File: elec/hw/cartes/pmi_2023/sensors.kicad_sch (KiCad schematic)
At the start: 44 parts, among them SW1 TQ2537A, SW2 TQ2537, SW6 TQ2537, SW9 TQ2537A, U10 tof_sensor_master, U13 GP2S60B, U14 GP2S60B, U15 GP2S60B, U16 GP2S60B, U19 GP2S60B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

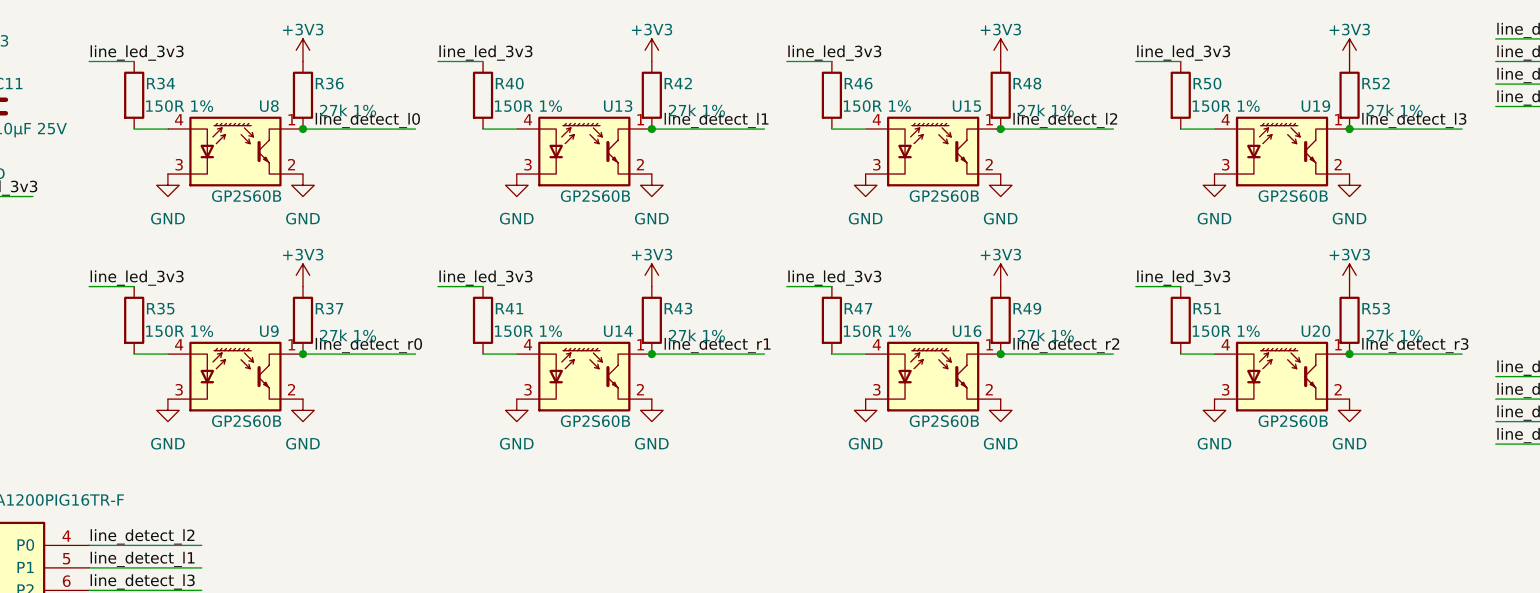
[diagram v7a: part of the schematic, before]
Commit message: GP2S60B replaced by ITR1204SR10A, RGB LED replaced by NH-B2020RGBA
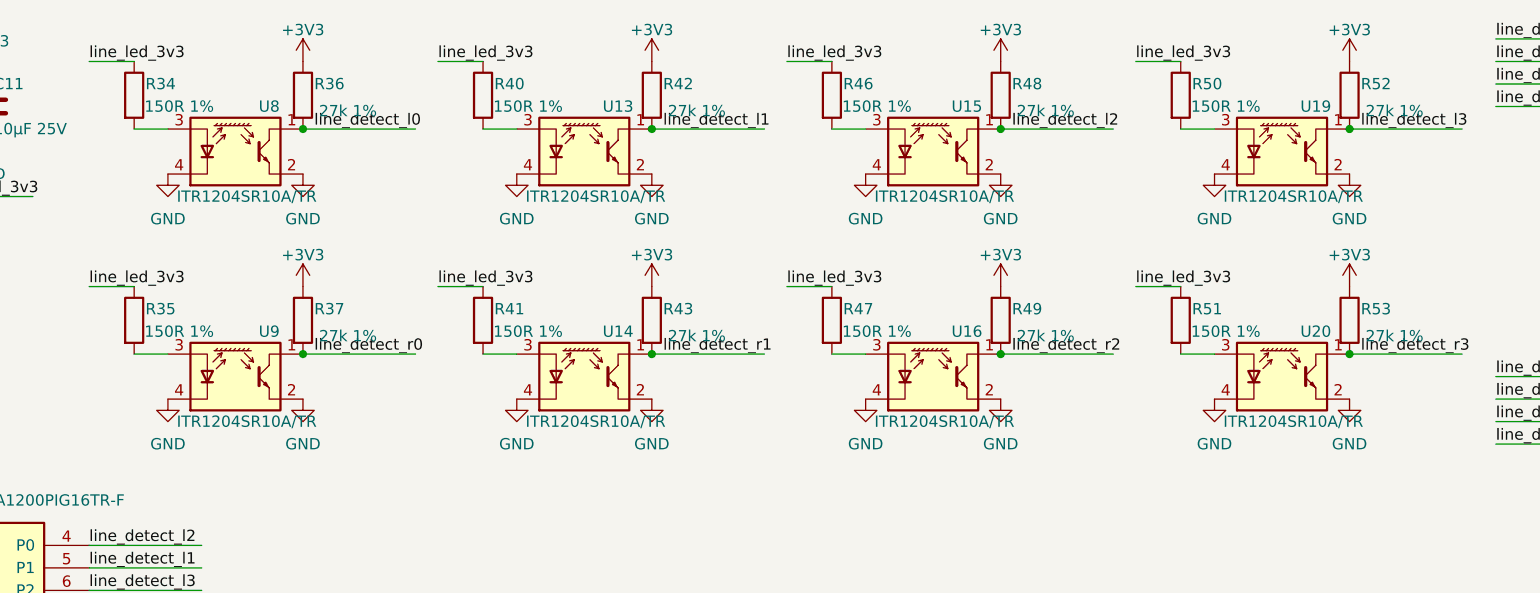
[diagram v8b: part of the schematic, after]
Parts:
- U13, U14, U15, U16, U19, U20, U8, U9: value GP2S60B -> ITR1204SR10A/TR; footprint cocotter_ic:GP2S60 -> cocotter_ic:ITR1204SR10A; symbol cocotter_ic:GP2S60B -> cocotter_ic:ITR1204SR10A/TR; JLCPCB C83485 -> C2943466
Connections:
- net GND: now also U13.4 (K), U14.4 (K), U15.4 (K), U16.4 (K), U19.4 (K), U20.4 (K), U8.4 (K), U9.4 (K); no longer U13.3 (K), U14.3 (K), U15.3 (K), U16.3 (K), U19.3 (K), U20.3 (K), U8.3 (K), U9.3 (K)
- net at R35.2: now also U9.3 (A); no longer U9.4 (A)
- net at R40.2: now also U13.3 (A); no longer U13.4 (A)
- net at R50.2: now also U19.3 (A); no longer U19.4 (A)
- net at R51.2: now also U20.3 (A); no longer U20.4 (A)
- net at R41.2: now also U14.3 (A); no longer U14.4 (A)
- net at R34.2: now also U8.3 (A); no longer U8.4 (A)
- net at R47.2: now also U16.3 (A); no longer U16.4 (A)
- net at R46.2: now also U15.3 (A); no longer U15.4 (A)
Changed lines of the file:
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@@
 	)
 	(symbol
-		(lib_id "cocotter_ic:GP2S60B")
+		(lib_id "cocotter_ic:ITR1204SR10A/TR")
 		(at 101.6 53.34 0)
 		(unit 1)
@@
 			)
 		)
-		(property "Value" "GP2S60B"
+		(property "Value" "ITR1204SR10A/TR"
 			(at 102.87 58.42 0)
 			(effects
@@
 			)
 		)
-		(property "Footprint" "cocotter_ic:GP2S60"
+		(property "Footprint" "cocotter_ic:ITR1204SR10A"
 			(at 101.6 53.34 0)
 			(effects
@@
 			)
 		)
-		(property "JLCPCB" "C83485"
+		(property "JLCPCB" "C2943466"
 			(at 101.6 53.34 0)
 			(effects
@@
 	)
 	(symbol
-		(lib_id "cocotter_ic:GP2S60B")
+		(lib_id "cocotter_ic:ITR1204SR10A/TR")
 		(at 140.97 27.94 0)
 		(unit 1)
@@
 			)
 		)
-		(property "Value" "GP2S60B"
+		(property "Value" "ITR1204SR10A/TR"
 			(at 142.24 33.02 0)
 			(effects
@@
 			)
 		)
-		(property "Footprint" "cocotter_ic:GP2S60"
+		(property "Footprint" "cocotter_ic:ITR1204SR10A"
 			(at 140.97 27.94 0)
 			(effects
@@
 			)
 		)
-		(property "JLCPCB" "C83485"
+		(property "JLCPCB" "C2943466"
 			(at 140.97 27.94 0)
 			(effects
@@
 	)
 	(symbol
-		(lib_id "cocotter_ic:GP2S60B")
+		(lib_id "cocotter_ic:ITR1204SR10A/TR")
 		(at 219.71 53.34 0)
 		(unit 1)
@@
 			)
 		)
-		(property "Value" "GP2S60B"
+		(property "Value" "ITR1204SR10A/TR"
 			(at 220.98 58.42 0)
 			(effects
@@
 			)
 		)
-		(property "Footprint" "cocotter_ic:GP2S60"
+		(property "Footprint" "cocotter_ic:ITR1204SR10A"
 			(at 219.71 53.34 0)
 			(effects
@@
 			)
 		)
-		(property "JLCPCB" "C83485"
+		(property "JLCPCB" "C2943466"
 			(at 219.71 53.34 0)
 			(effects
@@
 	)
 	(symbol
-		(lib_id "cocotter_ic:GP2S60B")
+		(lib_id "cocotter_ic:ITR1204SR10A/TR")
 		(at 219.71 27.94 0)
 		(unit 1)
@@
 			)
 		)
-		(property "Value" "GP2S60B"
+		(property "Value" "ITR1204SR10A/TR"
 			(at 220.98 33.02 0)
 			(effects
@@
 			)
 		)
-		(property "Footprint" "cocotter_ic:GP2S60"
+		(property "Footprint" "cocotter_ic:ITR1204SR10A"
 			(at 219.71 27.94 0)
 			(effects
@@
 			)
 		)
-		(property "JLCPCB" "C83485"
+		(property "JLCPCB" "C2943466"
 			(at 219.71 27.94 0)
 			(effects
@@
 	)
 	(symbol
-		(lib_id "cocotter_ic:GP2S60B")
+		(lib_id "cocotter_ic:ITR1204SR10A/TR")
 		(at 140.97 53.34 0)
 		(unit 1)
@@
 			)
 		)
-		(property "Value" "GP2S60B"
+		(property "Value" "ITR1204SR10A/TR"
 			(at 142.24 58.42 0)
 			(effects
@@
 			)
 		)
-		(property "Footprint" "cocotter_ic:GP2S60"
+		(property "Footprint" "cocotter_ic:ITR1204SR10A"
 			(at 140.97 53.34 0)
 			(effects
@@
 			)
 		)
-		(property "JLCPCB" "C83485"
+		(property "JLCPCB" "C2943466"
 			(at 140.97 53.34 0)
 			(effects
@@
 	)
 	(symbol
-		(lib_id "cocotter_ic:GP2S60B")
+		(lib_id "cocotter_ic:ITR1204SR10A/TR")
 		(at 101.6 27.94 0)
 		(unit 1)
@@
 			)
 		)
-		(property "Value" "GP2S60B"
+		(property "Value" "ITR1204SR10A/TR"
 			(at 102.87 33.02 0)
 			(effects
@@
 			)
 		)
-		(property "Footprint" "cocotter_ic:GP2S60"
+		(property "Footprint" "cocotter_ic:ITR1204SR10A"
 			(at 101.6 27.94 0)
 			(effects
@@
 			)
 		)
-		(property "JLCPCB" "C83485"
+		(property "JLCPCB" "C2943466"
 			(at 101.6 27.94 0)
 			(effects
@@
 	)
 	(symbol
-		(lib_id "cocotter_ic:GP2S60B")
+		(lib_id "cocotter_ic:ITR1204SR10A/TR")
 		(at 180.34 27.94 0)
 		(unit 1)
@@
 			)
 		)
-		(property "Value" "GP2S60B"
+		(property "Value" "ITR1204SR10A/TR"
 			(at 181.61 33.02 0)
 			(effects
@@
 			)
 		)
-		(property "Footprint" "cocotter_ic:GP2S60"
+		(property "Footprint" "cocotter_ic:ITR1204SR10A"
 			(at 180.34 27.94 0)
 			(effects
@@
 			)
 		)
-		(property "JLCPCB" "C83485"
+		(property "JLCPCB" "C2943466"
 			(at 180.34 27.94 0)
 			(effects
@@
 	)
 	(symbol
-		(lib_id "cocotter_ic:GP2S60B")
+		(lib_id "cocotter_ic:ITR1204SR10A/TR")
 		(at 180.34 53.34 0)
 		(unit 1)
@@
 			)
 		)
-		(property "Value" "GP2S60B"
+		(property "Value" "ITR1204SR10A/TR"
 			(at 181.61 58.42 0)
 			(effects
@@
 			)
 		)
-		(property "Footprint" "cocotter_ic:GP2S60"
+		(property "Footprint" "cocotter_ic:ITR1204SR10A"
 			(at 180.34 53.34 0)
 			(effects
@@
 			)
 		)
-		(property "JLCPCB" "C83485"
+		(property "JLCPCB" "C2943466"
 			(at 180.34 53.34 0)
 			(effects
